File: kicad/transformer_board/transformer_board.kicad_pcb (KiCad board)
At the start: 2 copper layers, 142.5 x 100 mm, 35 parts, among them J1 Conn_01x01, J2 Conn_01x01, J3 Conn_01x01, J4 Conn_01x01, J5 Conn_01x01, J6 Conn_01x01, J7 Conn_01x01, J8 Conn_01x01, J9 Conn_01x01, T1 14A-30-515, U1 LM317_TO-220, U2 LM337_TO220

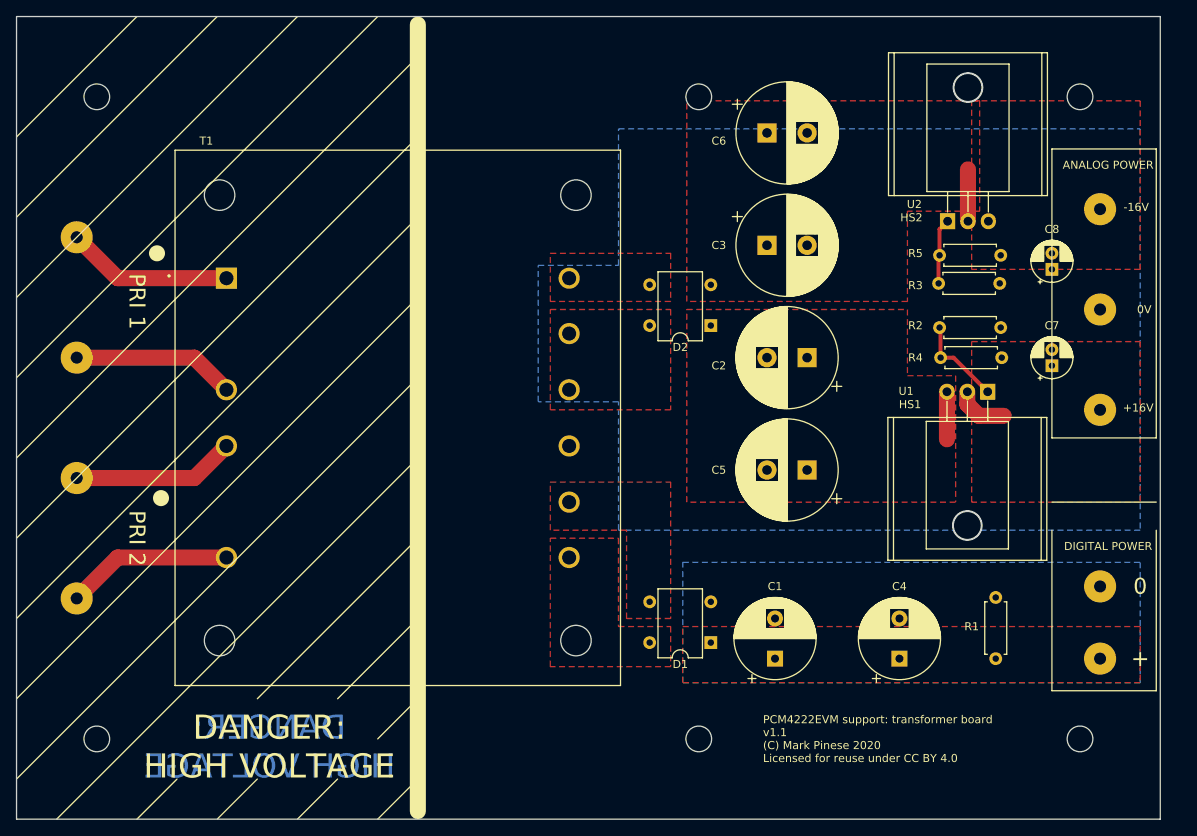
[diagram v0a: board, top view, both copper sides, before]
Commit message: Added preregs to all rails.
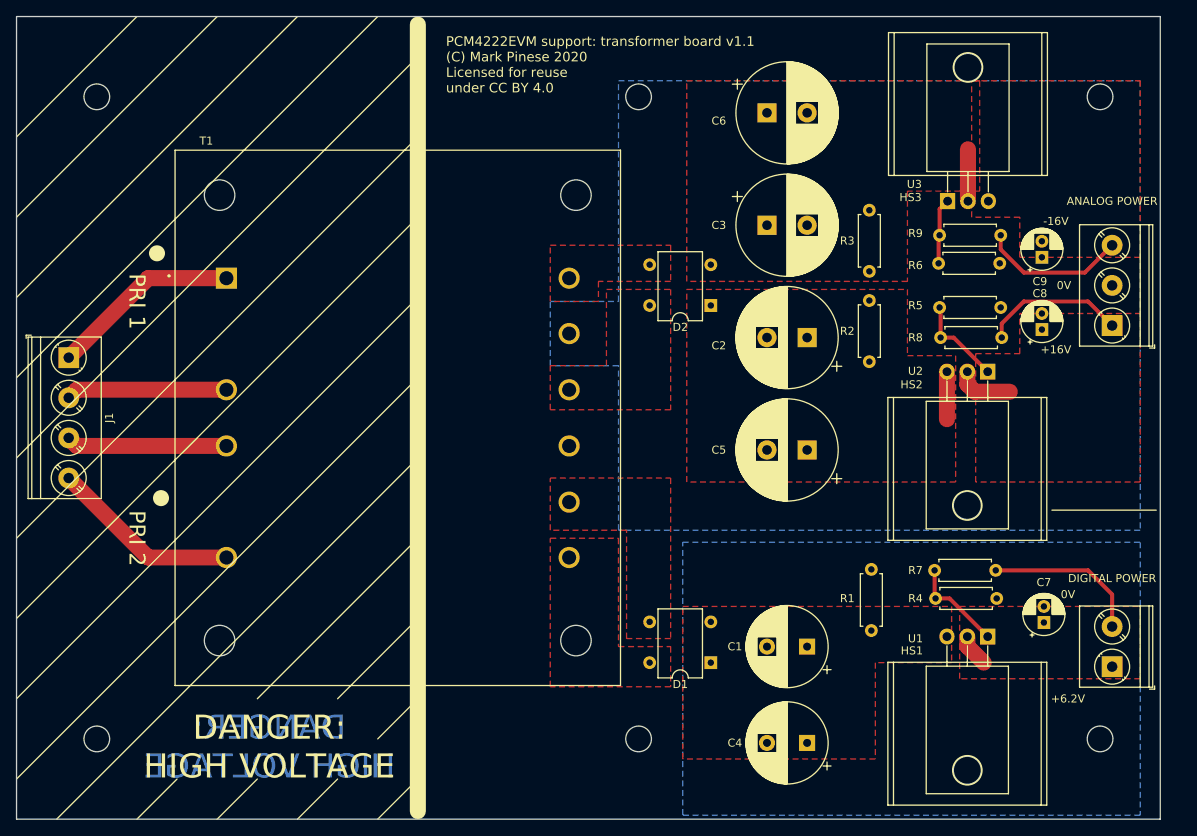
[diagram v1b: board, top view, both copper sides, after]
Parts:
- removed J4, J5, J6, J7, J8, J9: Conn_01x01, Connector_Wire:SolderWirePad_1x01_Drill1.5mm
- added C9: 10u, Capacitor_THT:CP_Radial_D5.0mm_P2.00mm, F.Cu at (202.8, 80.0)
- added HS3: Heatsink, project_footprints:AAVID_504102B00000G, F.Cu at (193.5, 60.9)
- added R6: 3.9k, Resistor_THT:R_Axial_DIN0207_L6.3mm_D2.5mm_P7.62mm_Horizontal, F.Cu at (197.5, 80.8)
- added R7: 330, Resistor_THT:R_Axial_DIN0207_L6.3mm_D2.5mm_P7.62mm_Horizontal, F.Cu at (197.0, 119.0)
- added R8: 330, Resistor_THT:R_Axial_DIN0207_L6.3mm_D2.5mm_P7.62mm_Horizontal, F.Cu at (197.8, 90.0)
- added R9: 330, Resistor_THT:R_Axial_DIN0207_L6.3mm_D2.5mm_P7.62mm_Horizontal, F.Cu at (190.0, 77.2)
- added U3: LM337_TO220, Package_TO_SOT_THT:TO-220-3_Horizontal_TabDown, F.Cu at (191.0, 73.0)
- J1: value Conn_01x01 -> Screw_Terminal_01x04; footprint Connector_Wire:SolderWirePad_1x01_Drill1.5mm -> TerminalBlock_Phoenix:TerminalBlock_Phoenix_PT-1,5-4-5.0-H_1x04_P5.00mm_Horizontal
- J2: value Conn_01x01 -> Screw_Terminal_01x02; footprint Connector_Wire:SolderWirePad_1x01_Drill1.5mm -> TerminalBlock_Phoenix:TerminalBlock_Phoenix_PT-1,5-2-5.0-H_1x02_P5.00mm_Horizontal
- J3: value Conn_01x01 -> Screw_Terminal_01x03; footprint Connector_Wire:SolderWirePad_1x01_Drill1.5mm -> TerminalBlock_Phoenix:TerminalBlock_Phoenix_PT-1,5-3-5.0-H_1x03_P5.00mm_Horizontal
- R2, R3: value 3.9k -> 10k
- R4: value 330 -> 1.3k
- R5: value 330 -> 3.9k
- U2: value LM337_TO220 -> LM317_TO-220
- moved J2 134.6 mm to (211.5, 131.0), turned to 90 degrees
- moved J3 130.4 mm to (211.5, 88.5), turned to 90 degrees
- moved HS2 43.0 mm to (193.5, 106.4), turned to 180 degrees
- moved C7 32.0 mm to (203.0, 125.5)
- moved R4 31.1 mm to (189.5, 122.5), turned to 0 degrees
- moved HS1 30.5 mm to (193.5, 139.3)
- moved U1 30.5 mm to (196.0, 127.2)
- moved U2 19.4 mm to (196.0, 94.2), turned to 180 degrees
- moved R3 16.3 mm to (181.2, 81.8), turned to 90 degrees
- moved R1 15.9 mm to (181.5, 126.5)
- moved C4 15.6 mm to (173.5, 140.5), turned to 180 degrees
- moved J1 15.0 mm to (81.5, 92.5), turned to 270 degrees
- moved R2 9.73 mm to (181.2, 93.0), turned to 90 degrees
- moved C8 7.60 mm to (202.8, 89.0)
- moved H3 7.50 mm to (152.5, 60.0)
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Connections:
- C7 pad 2: Net-(C2-Pad2) -> Net-(C1-Pad2)
- C8 pad 1: Net-(C2-Pad2) -> Net-(C8-Pad1)
- C8 pad 2: Net-(C8-Pad2) -> Net-(C2-Pad2)
- J2 pad 1: Net-(J2-Pad1) -> Net-(C1-Pad2)
- J3 pad 1: Net-(J3-Pad1) -> Net-(C8-Pad1)
- R2 pad 1: Net-(R2-Pad1) -> Net-(C2-Pad1)
- R3 pad 2: Net-(R3-Pad2) -> Net-(C3-Pad2)
- R4 pad 1: Net-(C7-Pad1) -> Net-(R4-Pad1)
- R4 pad 2: Net-(R2-Pad1) -> Net-(C1-Pad2)
- R5 pad 1: Net-(R3-Pad2) -> Net-(R5-Pad1)
- R5 pad 2: Net-(C8-Pad2) -> Net-(C2-Pad2)
- T1 pad 3: Net-(J2-Pad1) -> Net-(J1-Pad2)
- T1 pad 4: Net-(J3-Pad1) -> Net-(J1-Pad3)
- T1 pad 6: Net-(J4-Pad1) -> Net-(J1-Pad4)
- U1 pad 1: Net-(R2-Pad1) -> Net-(R4-Pad1)
- U1 pad 3: Net-(C2-Pad1) -> Net-(C1-Pad1)
- U2 pad 1: Net-(R3-Pad2) -> Net-(R5-Pad1)
- U2 pad 2: Net-(C3-Pad2) -> Net-(C8-Pad1)
- U2 pad 3: Net-(C8-Pad2) -> Net-(C2-Pad1)
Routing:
- net Net-(C8-Pad1): track 0.00 -> 25.1 mm
- net Net-(J1-Pad4): track 0.00 -> 23.8 mm
- net Net-(J4-Pad1): track 20.8 -> 0.00 mm
- net Net-(J1-Pad3): track 0.00 -> 20.4 mm
- net Net-(J3-Pad1): track 20.3 -> 0.00 mm
- net Net-(J2-Pad1): track 20.3 -> 0.00 mm
- net Net-(J1-Pad2): track 0.00 -> 20.1 mm
- net Net-(C9-Pad2): track 0.00 -> 18.3 mm
- net Net-(C7-Pad1): track 7.20 -> 23.8 mm
- net Net-(R4-Pad1): track 0.00 -> 13.1 mm
- net Net-(R5-Pad1): track 0.00 -> 11.4 mm
- net Net-(R2-Pad1): track 11.4 -> 0.00 mm
- net Net-(R6-Pad2): track 0.00 -> 8.21 mm
- net Net-(R3-Pad2): track 8.21 -> 0.00 mm
- net Net-(J1-Pad1): track 20.8 -> 23.8 mm
- added copper zone on F.Cu, net Net-(C8-Pad1)
- added copper zone on F.Cu, net Net-(C9-Pad2)
- removed copper zone on F.Cu, net Net-(C8-Pad2)
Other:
- board text added: "+6.2V"
- board text removed: "+"
- board text removed: "0"

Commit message: Fixed error in silkscreen
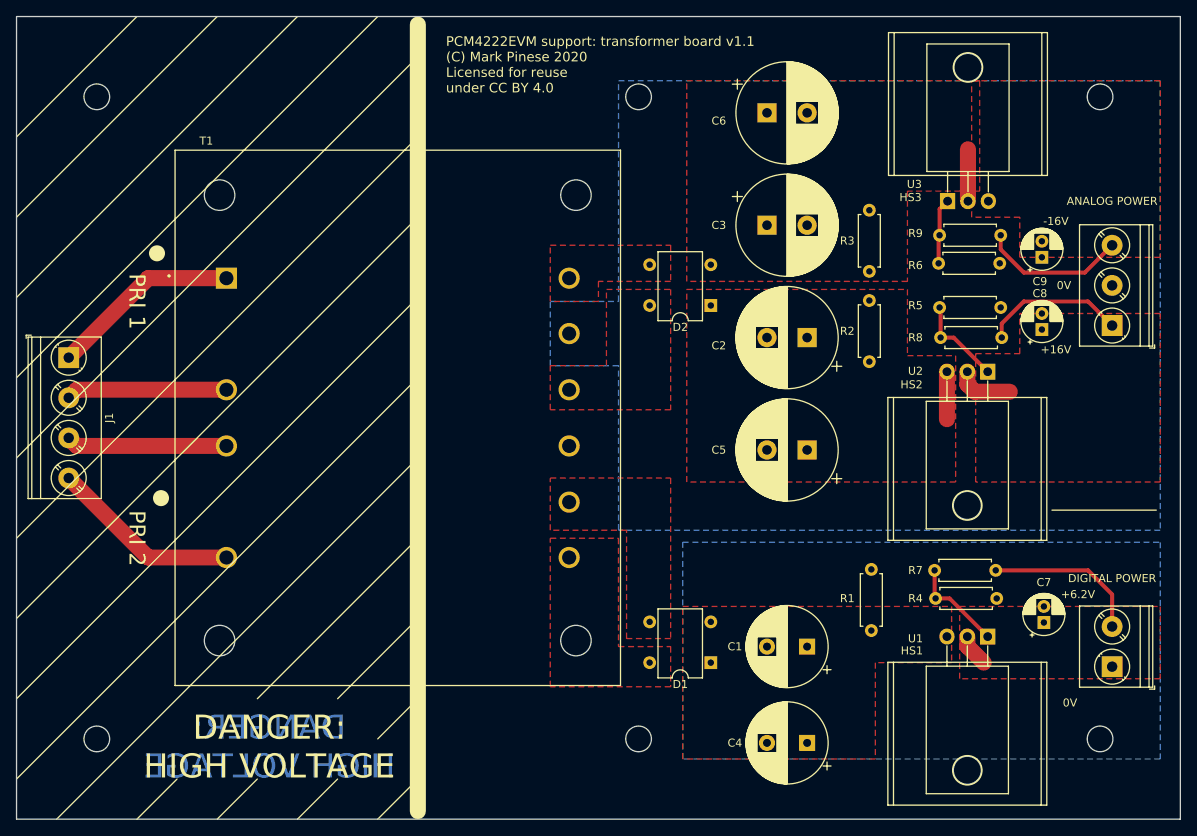
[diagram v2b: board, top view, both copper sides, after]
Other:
- board size 142.5 x 100 mm -> 145 x 100 mm
